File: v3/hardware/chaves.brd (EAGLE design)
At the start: 100 x 100 mm, 101 parts, among them IC1 40106N, J2 DCJ0202, T1 bc547, T2 bc547

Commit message: changing pinheaders to connect the trigger in properly
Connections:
- removed net N$20: C4.1, C5.1, IC1.3, R1.1
- removed net N$21: C6.1, C7.1, IC1.5, R2.1
- removed net N$31: C1.1, C2.1, IC1.1, R5.2
- removed net N$35: C8.1, C9.1, IC1.9, R3.1
- removed net N$36: C10.1, C11.1, IC1.11, R4.1
- removed net N$54: C12.1, C13.1, IC1.13, R8.2
- new net GNDA: U$1.2, U$2.2, U$3.2, U$4.2, U$5.2, U$6.2
- net SS1: now also C1.1, C2.1, IC1.1, R5.2; no longer U$1.2
- net SS2: now also C4.1, C5.1, IC1.3, R1.1; no longer U$2.2
- net SS3: now also C6.1, C7.1, IC1.5, R2.1; no longer U$3.2
- net SS4: now also C8.1, C9.1, IC1.9, R3.1; no longer U$4.2
- net SS5: now also C10.1, C11.1, IC1.11, R4.1; no longer U$5.2
- net SS6: now also C12.1, C13.1, IC1.13, R8.2; no longer U$6.2

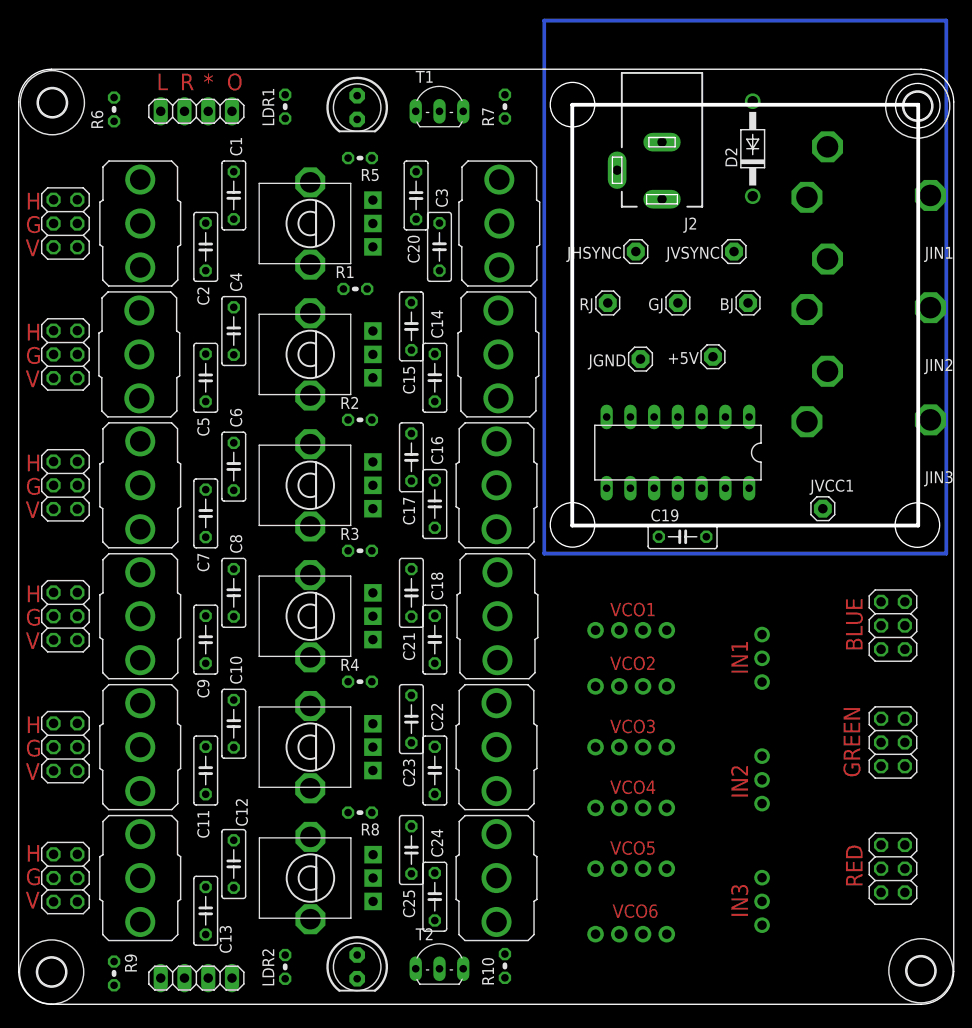
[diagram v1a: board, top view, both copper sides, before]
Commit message: Finixhed position and merged pins
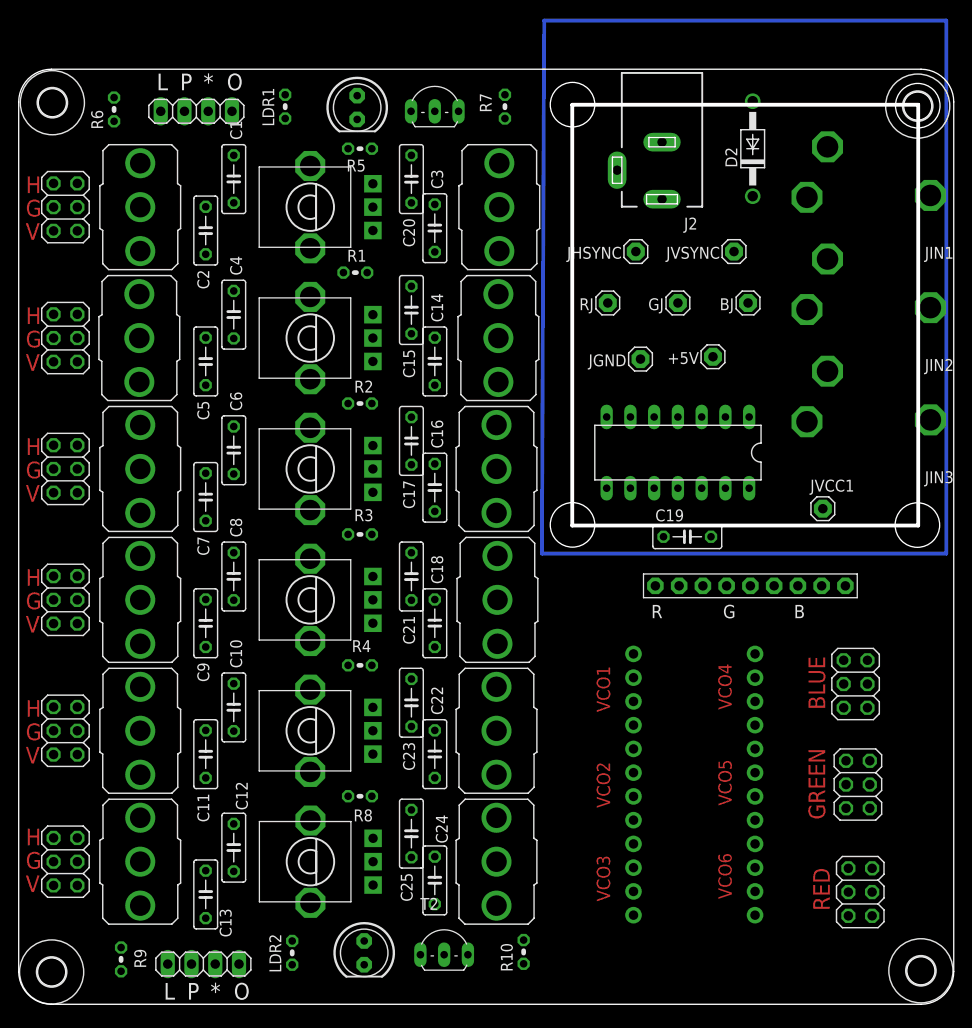
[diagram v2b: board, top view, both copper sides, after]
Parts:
- removed IN1, IN2, IN3: (no value), adafruit:1X03-CLEANBIG
- removed VCO1, VCO2, VCO3, VCO4, VCO5, VCO6: 1X4-CLEANBIG, adafruit:1X04-CLEANBIG
- added JP1: (no value), adafruit:1X09-BIG
- added O13, O45: (no value), adafruit:1X12-CB
- moved BLUE 7.42 mm to (89.5, 34.2)
- moved GREEN 5.86 mm to (89.8, 23.5)
- moved RED 4.30 mm to (90.0, 12.0)
- moved R10 2.50 mm to (54.0, 5.60)
- moved C3 2.06 mm to (44.5, 83.0)
- moved C20 1.82 mm to (42.0, 88.2)
- moved C1 1.75 mm to (23.0, 88.2)
- moved C10 1.75 mm to (23.0, 31.8)
- moved C11 1.75 mm to (20.0, 26.8)
- moved C12 1.75 mm to (23.0, 16.8)
- moved C13 1.75 mm to (20.0, 11.8)
- moved C14 1.75 mm to (44.5, 68.8)
- moved C15 1.75 mm to (42.0, 74.2)
- moved C16 1.75 mm to (44.5, 55.2)
- moved C17 1.75 mm to (42.0, 60.2)
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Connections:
- net VCC renamed VIN
- removed net N$14: GJ.1, GREEN.1, GREEN.2, GREEN.3, GREEN.4, GREEN.5, GREEN.6
- removed net N$15: BJ.1, BLUE.1, BLUE.2, BLUE.3, BLUE.4, BLUE.5, BLUE.6
- removed net N$18: U$7.2, VCO1.1, VCO1.2, VCO1.3, VCO1.4
- removed net N$25: IN1.1, IN1.2, IN1.3, JIN1.TIP
- removed net N$27: U$8.2, VCO2.1, VCO2.2, VCO2.3, VCO2.4
- removed net N$30: U$9.2, VCO3.1, VCO3.2, VCO3.3, VCO3.4
- removed net N$39: U$10.2, VCO4.1, VCO4.2, VCO4.3, VCO4.4
- removed net N$42: U$11.2, VCO6.1, VCO6.2, VCO6.3, VCO6.4
- removed net N$45: U$12.2, VCO5.1, VCO5.2, VCO5.3, VCO5.4
- new net BOUT: BJ.1, BLUE.1, BLUE.2, BLUE.3, BLUE.4, BLUE.5, BLUE.6, JP1.7
- new net GOUT: GJ.1, GREEN.1, GREEN.2, GREEN.3, GREEN.4, GREEN.5, GREEN.6, JP1.4
- new net N$20: JP8.2, JP8.4, JP8.6, U$1.2
- new net N$23: JP9.2, JP9.4, JP9.6, U$3.2
- new net N$31: JP10.2, JP10.4, JP10.6, U$4.2
- new net N$35: JP11.2, JP11.4, JP11.6, U$5.2
- new net N$36: JP12.2, JP12.4, JP12.6, U$6.2
- new net OUT1: O13.1, O13.2, O13.3, O13.4, U$7.2
- new net OUT2: O13.5, O13.6, O13.7, O13.8, U$8.2
- new net OUT3: O13.10, O13.11, O13.12, O13.9, U$9.2
- new net OUT4: O45.1, O45.2, O45.3, O45.4, U$10.2
- new net OUT5: O45.5, O45.6, O45.7, O45.8, U$11.2
- new net OUT6: O45.10, O45.11, O45.12, O45.9, U$12.2
- new net ROUT: JP1.1, RED.1, RED.2, RED.3, RED.4, RED.5, RED.6, RJ.1
- net GND: no longer JP10.3, JP11.3, JP12.3, JP3.3, JP8.3, JP9.3
- net GNDA: now also JP10.3, JP11.3, JP12.3, JP8.3, JP9.3; no longer U$1.2, U$3.2, U$4.2, U$5.2, U$6.2
- net N$12: now also JIN2.TIP, JP1.5, JP1.6; no longer IN3.1, IN3.2, IN3.3, JIN3.TIP
- net N$13: now also JIN3.TIP, JP1.8, JP1.9; no longer RED.1, RED.2, RED.3, RED.4, RED.5, RED.6, RJ.1
- net N$9: now also JIN1.TIP, JP1.2, JP1.3; no longer IN2.1, IN2.2, IN2.3, JIN2.TIP
- net SS1: no longer JP8.2, JP8.4, JP8.6
- net SS3: no longer JP9.2, JP9.4, JP9.6
- net SS4: no longer JP10.2, JP10.4, JP10.6
- net SS5: no longer JP11.2, JP11.4, JP11.6
- net SS6: no longer JP12.2, JP12.4, JP12.6
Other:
- board text added: "B"
- board text added: "CHA/V-ES basado en jonasbers.com/chav/"
- board text added: "Cha-Cha-CHAV!!"
- board text added: "P"
- board text removed: "CHAV/ES - based on jonasbers.com/chav/"
- board text removed: "IN1"
- board text removed: "IN2"
- board text removed: "IN3"

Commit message: fully routed v3, checked errors, layers corrected ready to fav proto
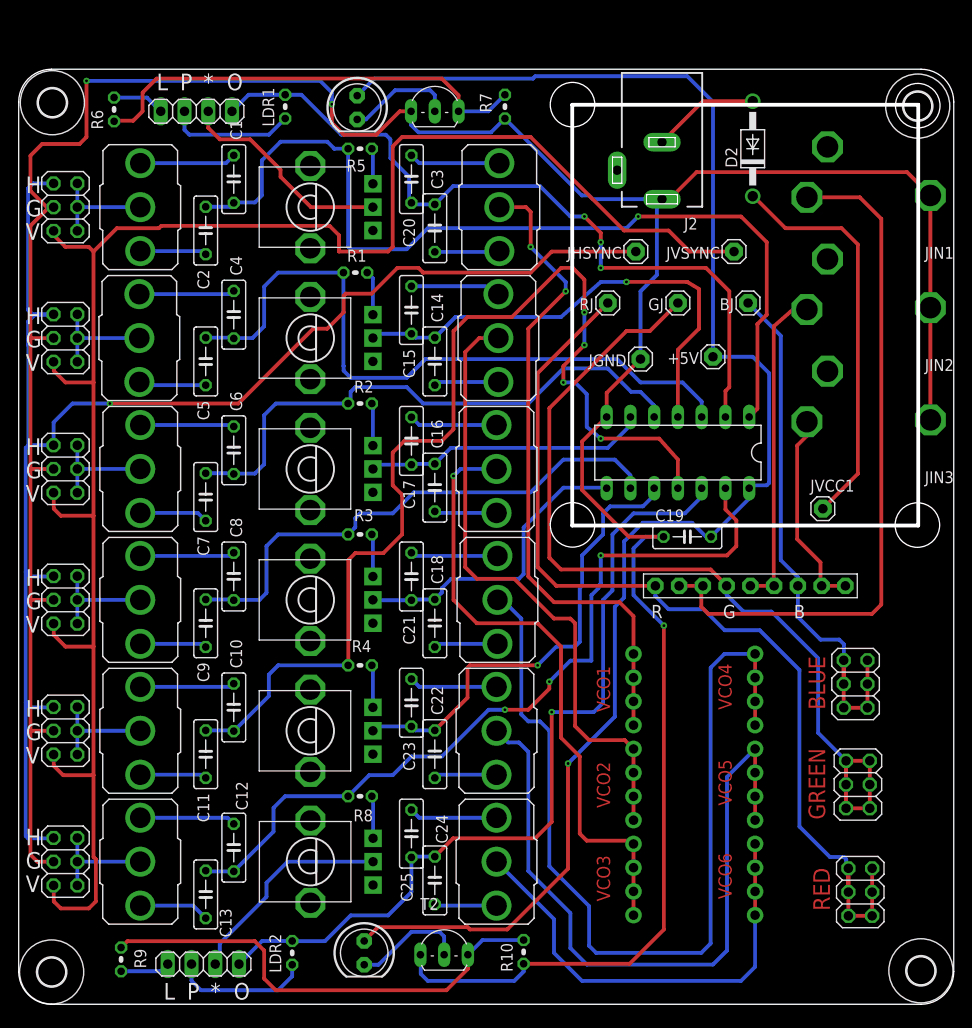
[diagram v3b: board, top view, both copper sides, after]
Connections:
- removed net GNDA: JP10.3, JP11.3, JP12.3, JP8.3, JP9.3, U$2.2
- new net N$14: JP3.2, JP3.4, JP3.6, U$2.2
- net GND: now also JP10.3, JP11.3, JP12.3, JP3.3, JP8.3, JP9.3
- net SS2: no longer JP3.2, JP3.4, JP3.6
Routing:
- net GND: track 0.00 -> 353.2 mm, vias 0 -> 3
- net S$1: track 200.3 -> 0.00 mm
- net VSYNC: track 0.00 -> 194.0 mm
- net +5V: track 0.00 -> 168.5 mm, vias 0 -> 1
- net HSYNC: track 0.00 -> 163.0 mm, vias 0 -> 1
- net SS5: track 0.00 -> 114.9 mm, vias 0 -> 4
- net ROUT: track 0.00 -> 104.1 mm
- net OUT4: track 0.00 -> 98.3 mm
- net GOUT: track 0.00 -> 98.2 mm
- net SS1: track 0.00 -> 98.0 mm, vias 0 -> 1
- net N$55: track 0.00 -> 90.1 mm, vias 0 -> 1
- net SS6: track 0.00 -> 85.8 mm, vias 0 -> 3
- net N$101: track 0.00 -> 82.7 mm, vias 0 -> 3
- net OUT5: track 0.00 -> 75.7 mm
- net N$9: track 0.00 -> 75.0 mm
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
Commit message: Revised gerbers for all versions
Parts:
- removed J2: DCJ0202, con-jack:DCJ0202
- added CN1: (no value), adafruit:DCJACK_2MM_PTH
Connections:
- new net GNDBREAK: CN1.GNDBREAK
- net GND: now also CN1.GND; no longer J2.1
- net VIN: now also CN1.PWR; no longer J2.3
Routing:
- net GND: track 353.2 -> 373.1 mm
- net VIN: track 11.5 -> 15.8 mm
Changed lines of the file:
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@@
 <attribute name="NAME" x="100" y="81" size="1.27" layer="25" font="vector" rot="R180"/>
-</element>
-<element name="J2" library="con-jack" package="DCJ0202" value="DCJ0202" x="68.8" y="89.2" smashed="yes" rot="R180">
-<attribute name="NAME" x="72.61" y="84.12" size="1.27" layer="25" font="vector" rot="R180"/>
-<attribute name="VALUE" x="73.88" y="99.36" size="1.27" layer="27" font="vector" rot="R270"/>
 </element>
 <element name="D2" library="diode" package="DO41-10" value="1N4004" x="78.5" y="91.5" smashed="yes" rot="R90">
@@
 <attribute name="VALUE" x="68.09" y="41.575" size="1.27" layer="27"/>
 </element>
+<element name="CN1" library="adafruit" package="DCJACK_2MM_PTH" value="" x="70" y="100" rot="R180"/>
 </elements>
 <signals>
@@
 <contactref element="T2" pad="E"/>
 <contactref element="JIN1" pad="GND"/>
-<contactref element="J2" pad="1"/>
 <contactref element="C19" pad="1"/>
 <contactref element="JIN2" pad="GND"/>
@@
 <wire x1="97.5" y1="74.5" x2="97.5" y2="62.5" width="0.4064" layer="1"/>
 <wire x1="97.5" y1="86.5" x2="95" y2="89" width="0.4064" layer="1"/>
-<wire x1="95" y1="89" x2="72.5" y2="89" width="0.4064" layer="1"/>
-<wire x1="72.5" y1="89" x2="69.6" y2="86.1" width="0.4064" layer="1"/>
-<wire x1="69.6" y1="86.1" x2="68.8" y2="86.1" width="0.4064" layer="1"/>
 <wire x1="62.88" y1="62.81" x2="62.88" y2="65.38" width="0.4064" layer="1"/>
 <wire x1="62.88" y1="65.38" x2="66.5" y2="69" width="0.4064" layer="1"/>
 <wire x1="66.5" y1="69" x2="66.5" y2="76.25" width="0.4064" layer="16"/>
 <wire x1="66.5" y1="76.25" x2="68.25" y2="78" width="0.4064" layer="16"/>
-<wire x1="68.25" y1="78" x2="68.25" y2="85.55" width="0.4064" layer="16"/>
-<wire x1="68.25" y1="85.55" x2="68.8" y2="86.1" width="0.4064" layer="16"/>
-<wire x1="68.8" y1="86.1" x2="61.4" y2="86.1" width="0.4064" layer="16"/>
-<wire x1="61.4" y1="86.1" x2="61" y2="86.5" width="0.4064" layer="16"/>
-<wire x1="61" y1="86.5" x2="60.23" y2="86.5" width="0.4064" layer="16"/>
-<wire x1="60.23" y1="86.5" x2="52" y2="94.73" width="0.4064" layer="16"/>
+<wire x1="60.23" y1="86.5" x2="57.115" y2="89.615" width="0.4064" layer="16"/>
+<wire x1="57.115" y1="89.615" x2="52" y2="94.73" width="0.4064" layer="16"/>
 <wire x1="54" y1="4.33" x2="65.33" y2="4.33" width="0.4064" layer="1"/>
 <wire x1="65.33" y1="4.33" x2="69" y2="8" width="0.4064" layer="1"/>
@@
 <wire x1="38.25" y1="93" x2="40.75" y2="95.5" width="0.4064" layer="1"/>
 <wire x1="40.75" y1="95.5" x2="41.96" y2="95.5" width="0.4064" layer="1"/>
+<contactref element="CN1" pad="GND"/>
+<wire x1="60.23" y1="86.5" x2="60.25" y2="86.5" width="0.4064" layer="16"/>
+<wire x1="60.25" y1="86.5" x2="61" y2="85.75" width="0.4064" layer="16"/>
+<wire x1="61" y1="85.75" x2="66.25" y2="85.75" width="0.4064" layer="16"/>
+<wire x1="66.25" y1="85.75" x2="68.25" y2="83.75" width="0.4064" layer="16"/>
+<wire x1="68.25" y1="83.75" x2="68.25" y2="78" width="0.4064" layer="16"/>
+<wire x1="95" y1="89" x2="92.5" y2="89" width="0.4064" layer="1"/>
+<wire x1="92.5" y1="89" x2="91" y2="90.5" width="0.4064" layer="1"/>
+<wire x1="91" y1="90.5" x2="91" y2="97.25" width="0.4064" layer="1"/>
+<wire x1="91" y1="97.25" x2="89.75" y2="98.5" width="0.4064" layer="1"/>
+<wire x1="89.75" y1="98.5" x2="75.85" y2="98.5" width="0.4064" layer="1"/>
+<wire x1="75.85" y1="98.5" x2="70" y2="92.65" width="0.4064" layer="1"/>
+<wire x1="70" y1="92.65" x2="60.15" y2="92.65" width="0.4064" layer="16"/>
+<wire x1="60.15" y1="92.65" x2="57.115" y2="89.615" width="0.4064" layer="16"/>
 </signal>
 <signal name="N$32">
@@
 </signal>
 <signal name="VIN">
-<contactref element="J2" pad="3"/>
 <contactref element="D2" pad="A"/>
-<wire x1="68.8" y1="92.2" x2="73.18" y2="96.58" width="0.4064" layer="1"/>
-<wire x1="73.18" y1="96.58" x2="78.5" y2="96.58" width="0.4064" layer="1"/>
+<contactref element="CN1" pad="PWR"/>
+<wire x1="70" y1="86.4" x2="73.65" y2="86.4" width="0.4064" layer="1"/>
+<wire x1="73.65" y1="86.4" x2="78.5" y2="91.25" width="0.4064" layer="1"/>
+<wire x1="78.5" y1="91.25" x2="78.5" y2="96.58" width="0.4064" layer="1"/>
 </signal>
 <signal name="N$62">
@@
 <wire x1="6.27" y1="71.25" x2="12.9" y2="71.25" width="0.4064" layer="16"/>
 </signal>
+<signal name="GNDBREAK">
+<contactref element="CN1" pad="GNDBREAK"/>
+</signal>
 </signals>
